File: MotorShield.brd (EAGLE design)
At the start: 85 x 56 mm, 119 parts, among them IC1 OPA4340E, IC2 OPA4340E, IC3 74HCT125D, T1 FDN337N, T2 FDN337N, T3 FDN337N, T4 FDN337N, T5 FDN337N, T6 FDN337N, T7 FDN337N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

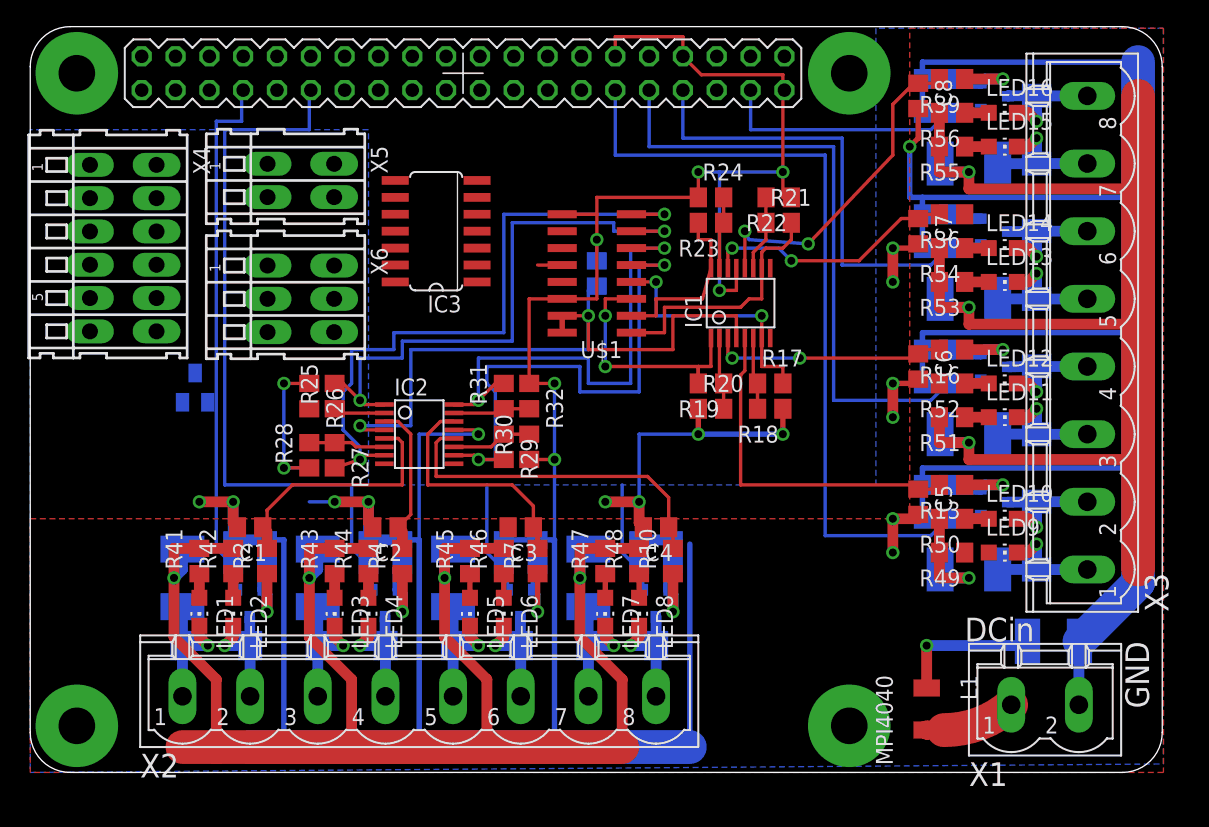
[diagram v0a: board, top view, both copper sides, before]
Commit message: completely changed wiring of GPIOs https://github.com/IUNO-TDM/PumpControl/issues/27 https://github.com/IUNO-TDM/MotorShield/issues/11
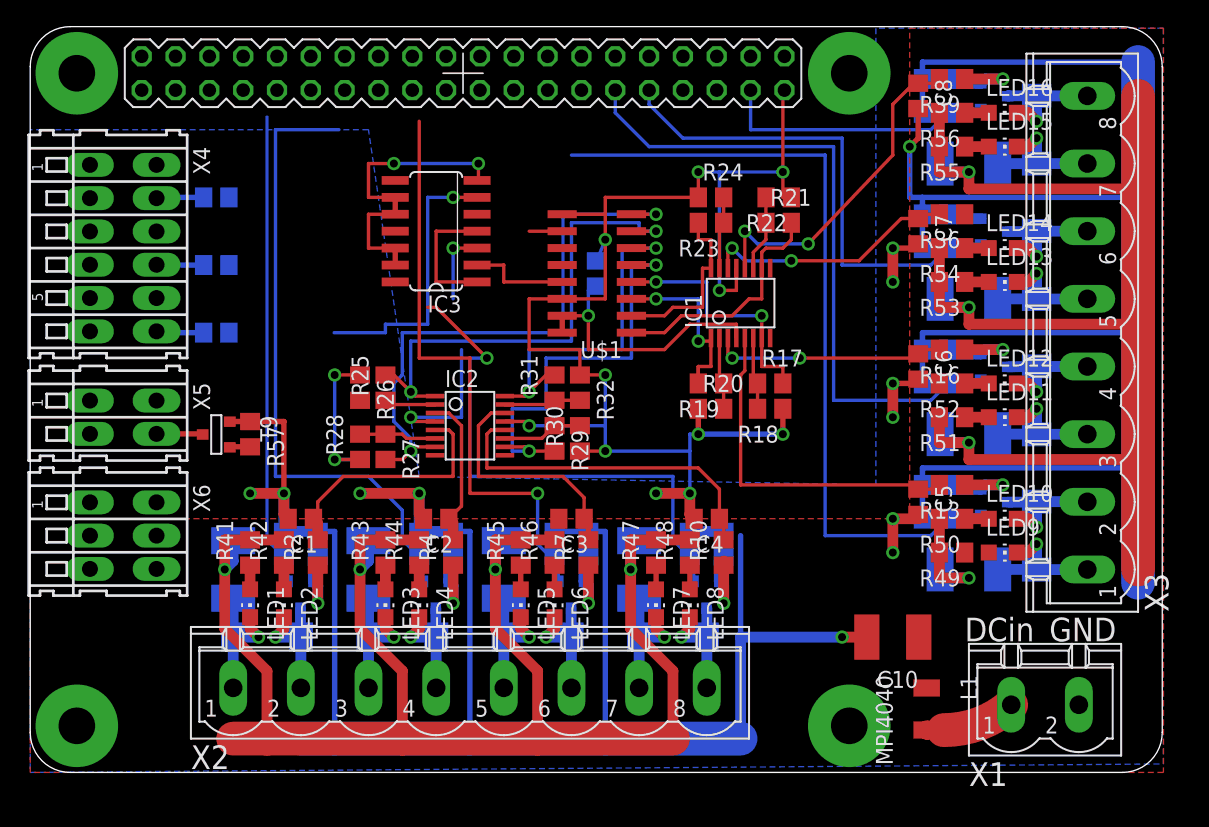
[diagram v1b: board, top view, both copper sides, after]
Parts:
- added R57: 10k, rcl:R0805
- added R58, R59, R60: 220, rcl:R0805
- T9: value BC847C -> FDN337N; device transistor:SOT23-BEC -> zetex:SOT-23
- moved X5 22.2 mm to (6.99, 26.7)
- moved X6 22.2 mm to (6.99, 17.8)
- moved C10 12.1 mm to (64.8, 10.2), flipped to the top
- moved C3 3.86 mm to (40.6, 19.1)
- moved IC2 3.86 mm to (33.0, 26.0)
- moved R10 3.86 mm to (52.1, 16.5)
- moved R27 3.86 mm to (26.7, 24.4)
- moved R28 3.86 mm to (24.8, 24.4)
- moved R41 3.86 mm to (16.5, 16.5)
- moved R43 3.86 mm to (26.7, 16.5)
- moved R44 3.86 mm to (29.2, 16.5)
- moved R47 3.86 mm to (47.0, 16.5)
- moved R48 3.86 mm to (49.5, 16.5)
- moved T3 3.86 mm to (40.6, 13.3)
- moved D2 3.86 mm to (27.9, 10.2)
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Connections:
- removed net CLK: IC3.2, PCB1.23, U$1.13
- removed net DIN: IC3.5, PCB1.19, U$1.11
- removed net DOUT: PCB1.21, U$1.12
- removed net SPI0CE1: IC3.1, IC3.4
- new net BTN_LED: PCB1.18, R57.2, T9.3
- new net GPIO07: PCB1.26
- new net GPIO08: PCB1.24
- new net GPIO10: PCB1.19
- new net GPIO11: PCB1.23
- new net N$60: R59.2, X4.A4
- new net N$61: R60.2, X4.A6
- new net PWM0: PCB1.32
- new net PWM1: PCB1.33
- new net RXD0: PCB1.10
- new net SPI1_CE2: PCB1.36
- new net SPI1_MISO: PCB1.35, U$1.12
- new net SPI1_MOSI: IC3.5, PCB1.38, U$1.11
- new net SPI1_SCLK: IC3.2, PCB1.40, U$1.13
- new net TXD0: PCB1.8
- net CS_ADC: now also PCB1.12; no longer PCB1.24
- net CS_DOTSTARS: now also IC3.1, IC3.4, PCB1.11; no longer PCB1.26
- net GND: now also R57.1, R58.1, R59.1, R60.1, T9.2; no longer T9.E, X4.A2, X4.A4, X4.A6
- net INP_BTN_START: now also PCB1.7
- net INP_DOOR_CTRL: now also PCB1.16
- net INP_DOOR_JUICE: now also PCB1.15
- net M1: now also PCB1.31; no longer PCB1.33
- net M2: now also PCB1.29; no longer PCB1.31
- net M3: no longer PCB1.29
- net M4: no longer PCB1.15
- net M5: no longer PCB1.16
- net M6: now also PCB1.21; no longer PCB1.11
- net M7: now also PCB1.22; no longer PCB1.7
- net N$32: now also T9.1; no longer T9.C
- net N$33: now also R58.2, X4.A2; no longer T9.B
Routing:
- net M5: track 8.70 -> 44.3 mm, vias 0 -> 1
- net M4: track 8.70 -> 39.9 mm, vias 0 -> 1
- net DOTDAT: track 0.00 -> 20.9 mm, vias 0 -> 1
- net +3V3: track 51.3 -> 32.4 mm
- net +24V: track 249.5 -> 238.6 mm, vias 9 -> 8
- net CS_DOTSTARS: track 0.00 -> 9.96 mm
- net CH5: track 36.1 -> 26.6 mm
- net SPI1_SCLK: track 0.00 -> 7.66 mm
- net CH4: track 40.3 -> 33.0 mm
- net GND: track 421.5 -> 428.6 mm, vias 24 -> 27
- net M6: track 54.1 -> 47.4 mm
- net CH6: track 43.7 -> 38.0 mm
- net DOTCLK: track 0.00 -> 5.61 mm, vias 0 -> 1
- net CH7: track 49.1 -> 43.6 mm
- net M7: track 40.2 -> 35.5 mm
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
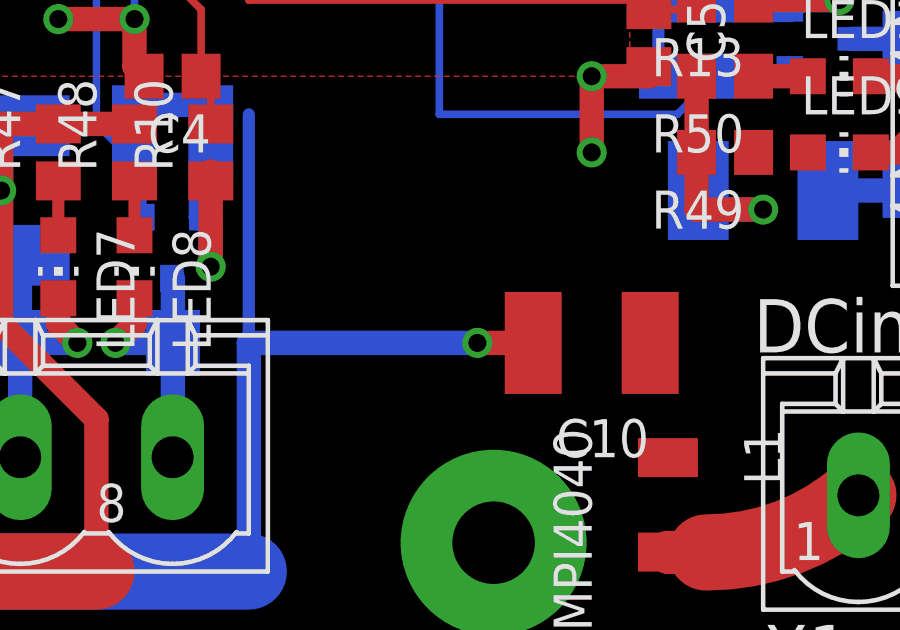
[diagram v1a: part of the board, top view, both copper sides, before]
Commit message: added power indicator led
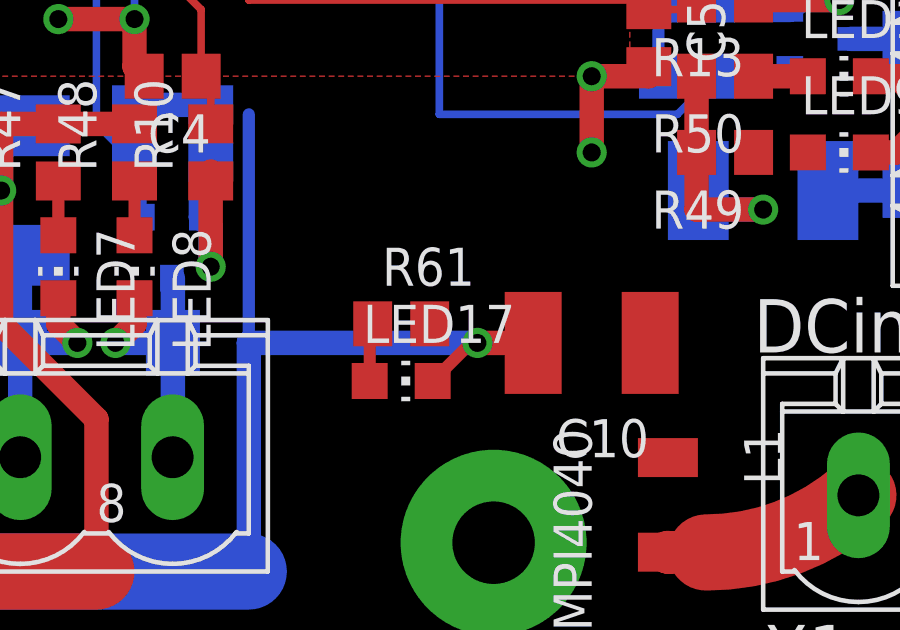
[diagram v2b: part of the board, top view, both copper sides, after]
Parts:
- added LED17: green, led:CHIP-LED0805
- added R61: 2k2, rcl:R0805
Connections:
- new net N$62: LED17.A, R61.1
- net +24V: now also R61.2
- net GND: now also LED17.C
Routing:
- net N$62: track 0.00 -> 2.98 mm
- net GND: track 428.6 -> 430.6 mm
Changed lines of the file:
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@@
 <element name="R59" library="rcl" package="R0805" value="220" x="13.97" y="38.1" rot="MR0"/>
 <element name="R60" library="rcl" package="R0805" value="220" x="13.97" y="33.02" rot="MR0"/>
+<element name="LED17" library="led" package="CHIP-LED0805" value="green" x="58.42" y="8.89" rot="R270"/>
+<element name="R61" library="rcl" package="R0805" value="2k2" x="58.42" y="10.795"/>
 </elements>
 <signals>
@@
 <wire x1="16.51" y1="26.35" x2="19.05" y2="26.35" width="0.4064" layer="1"/>
 <wire x1="19.05" y1="26.35" x2="19.05" y2="20.955" width="0.4064" layer="1"/>
+<contactref element="LED17" pad="C"/>
+<wire x1="60.96" y1="10.16" x2="60.74" y2="10.16" width="0.4064" layer="1"/>
+<wire x1="60.74" y1="10.16" x2="59.47" y2="8.89" width="0.4064" layer="1"/>
 <wire x1="43.93" y1="53.77" x2="49.01" y2="53.77" width="0" layer="19" extent="1-1"/>
 <wire x1="38.85" y1="51.23" x2="43.93" y2="53.77" width="0" layer="19" extent="1-1"/>
@@
 <via x="70.485" y="45.085" extent="1-16" drill="0.6" shape="square"/>
 <wire x1="19.05" y1="17.46" x2="16.51" y2="17.46" width="0.8128" layer="1"/>
+<contactref element="R61" pad="2"/>
 <wire x1="14.605" y1="17.46" x2="9.485" y2="27.92" width="0" layer="19" extent="1-1"/>
 </signal>
@@
 <wire x1="9.485" y1="33.02" x2="9.485" y2="33.12" width="0.4064" layer="16"/>
 </signal>
+<signal name="N$62">
+<contactref element="LED17" pad="A"/>
+<contactref element="R61" pad="1"/>
+<wire x1="57.37" y1="8.89" x2="57.37" y2="11.33" width="0.4064" layer="1"/>
+<wire x1="57.37" y1="11.33" x2="57.47" y2="10.795" width="0.4064" layer="1"/>
+</signal>
 </signals>

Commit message: finished routing, no more airwires :)
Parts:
- moved C9 1.27 mm to (41.3, 37.5)
- moved C8 0.90 mm to (66.0, 50.2)
- moved C1 0.63 mm to (20.3, 19.7)
- moved C2 0.63 mm to (30.5, 19.7)
- moved C3 0.63 mm to (40.6, 19.7)
- moved C4 0.63 mm to (50.8, 19.7)
- moved C5 0.63 mm to (66.0, 20.3)
- moved C6 0.63 mm to (66.0, 30.5)
- moved C7 0.63 mm to (66.0, 40.6)
- renumbered U$1 to IC4
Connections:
- removed net GPIO07: PCB1.26
- removed net GPIO08: PCB1.24
- removed net GPIO11: PCB1.23
- net M3: now also PCB1.26
- net M4: now also PCB1.23
- net M5: now also PCB1.24
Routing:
- net BTN_LED: track 1.56 -> 47.0 mm
- net DOTCLK: track 5.61 -> 46.6 mm, vias 1 -> 3
- net SPI1_MOSI: track 0.00 -> 34.6 mm
- net DOTDAT: track 20.9 -> 54.7 mm, vias 1 -> 3
- net VCC: track 0.00 -> 33.1 mm, vias 0 -> 2
- net SPI1_SCLK: track 7.66 -> 40.7 mm
- net INP_DOOR_JUICE: track 0.00 -> 31.9 mm
- net INP_DOOR_CTRL: track 0.00 -> 29.8 mm
- net CS_ADC: track 2.48 -> 32.0 mm, vias 0 -> 1
- net +3V3: track 32.4 -> 5.73 mm, vias 2 -> 1
- net CS_DOTSTARS: track 9.96 -> 35.1 mm, vias 0 -> 1
- net GND: track 430.6 -> 406.6 mm, vias 27 -> 29
- net SPI1_MISO: track 0.00 -> 23.9 mm
- net +24V: track 238.6 -> 259.2 mm
- net M7: track 35.5 -> 54.7 mm
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- added copper zone on layer 1, net +3V3
- added copper zone on layer 1, net GND

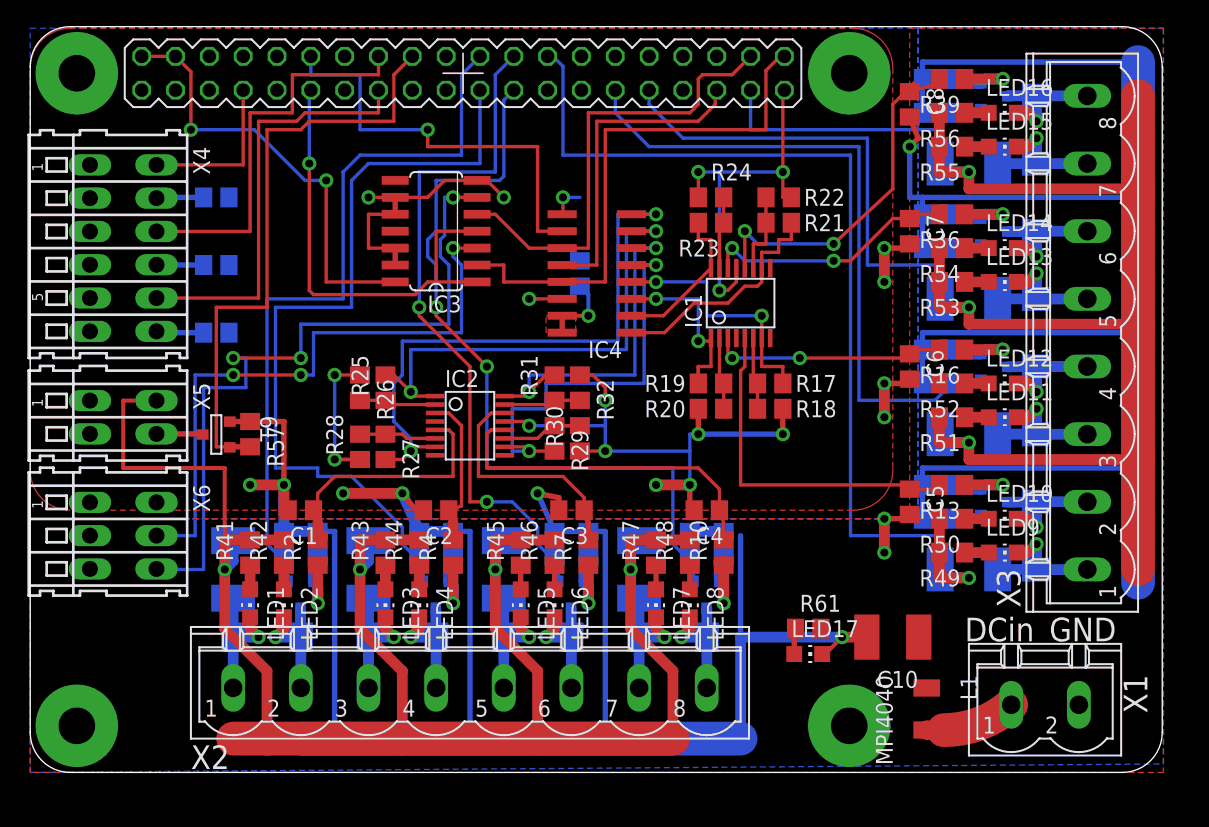
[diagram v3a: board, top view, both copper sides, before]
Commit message: shrunk most vias
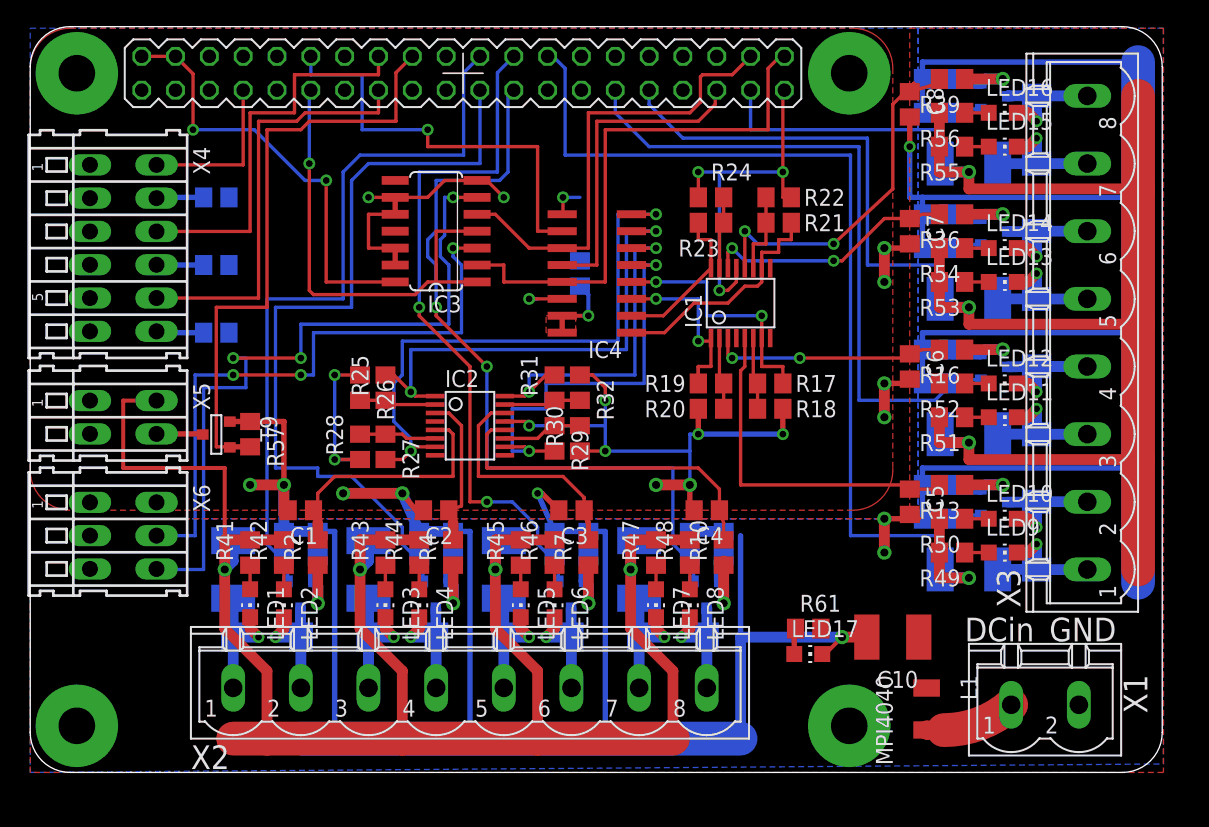
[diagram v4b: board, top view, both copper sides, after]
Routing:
- net GND: track 406.6 -> 405.7 mm

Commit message: revised routing
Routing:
- net GND: track 405.7 -> 372.5 mm
- net +24V: track 259.2 -> 246.1 mm
- net INP_DOOR_JUICE: track 31.9 -> 24.6 mm
- net INP_DOOR_CTRL: track 29.8 -> 24.5 mm
- net BTN_LED: track 47.1 -> 41.8 mm
- net DOTCLK: track 46.6 -> 49.7 mm
- net SPI1_SCLK: track 40.8 -> 38.3 mm
- net INP_BTN_START: track 12.1 -> 10.0 mm
- net CS_DOTSTARS: track 35.1 -> 33.1 mm
- net V3: track 27.8 -> 25.9 mm
- net CH7: track 43.6 -> 41.8 mm
- net V0: track 27.8 -> 26.2 mm
- net M5: track 52.2 -> 50.9 mm
- net CH6: track 36.7 -> 35.6 mm
- net CH5: track 26.6 -> 25.7 mm
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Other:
- board text added: "Jan Rauser Hans-Peter Bock"
- board text added: "TRUMPF Werkzeugmaschinen GmbH + Co. KG"
- board text added: "V+"
- board text removed: "DCin"
